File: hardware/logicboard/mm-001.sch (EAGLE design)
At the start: 31 parts, among them IC1 74ALS05N, IC2 LTC485N, IC3 LTC485N, J0 DC5V, J7 DIN5, J8 DIN5, J9 DIN5, X7 NELTRON-7810-XPXC, X9 NELTRON-7810-XPXC

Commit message: Trying to fit in to the new platform.
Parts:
- removed J0: DC5V, con-jack:JACK-PLUG0
- removed J7, J8, J9: DIN5, SparkFun-Connectors:DIN5
- removed LED1: BLUE, led:LED3MM
- removed LED2, LED3: YELLOW, led:LED3MM
- removed R7L2, R8L3: 1k, rcl:R-EU_0204/5
- removed X7, X9: NELTRON-7810-XPXC, con-rj45:NELTRON-7810-XPXC
- added JP1, JP2: (no value), pinhead:PINHD-1X6
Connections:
- removed net MTRTN: J8.5, R5.1
- removed net MTSND: J8.4, R4.1
- removed net N$1: IC1C.O, LED2.C
- removed net N$2: LED3.A, R8L3.1
- removed net N$3: IC1F.O, LED3.C
- removed net N$5: LED2.A, R7L2.1
- net GND: now also JP1.1, JP2.1; no longer J0.1, J0.2, J8.2, J9.2, LED1.C, X7.S1, X7.S2, X9.S1, X9.S2
- net MIRTN: now also JP1.4; no longer J7.5
- net MISND: now also JP1.3; no longer J7.4
- net MORTN: now also JP1.6; no longer J9.5
- net MOSND: now also JP1.5; no longer J9.4
- net N$4: now also JP2.2; no longer LED1.A
- net RX+: now also JP2.5; no longer X7.1
- net RX-: now also JP2.6; no longer X7.2
- net TX+: now also JP2.3; no longer X9.1
- net TX-: now also JP2.4; no longer X9.2
- net VCC: now also JP1.2; no longer J0.3, R7L2.2, R8L3.2
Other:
- moved on the sheet: R6L1

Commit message: First try.
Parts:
- removed R5: 220, rcl:R-EU_0204/5
- R4: value 220 -> 100
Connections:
- removed net MIDITHRU: IC1B.O, R5.2
- removed net NMIDITHRU: IC1A.O, IC1B.I, RN2.3
- net GND: now also IC1A.I, IC1B.I, IC1C.I, IC1F.I
- net RX: no longer IC1F.I
- net TX: no longer IC1A.I, IC1C.I
- net TX+: now also R4.1
- net TX-: now also R4.2
- net VCC: no longer R4.2
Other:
- moved on the sheet: IC1A, IC1B, IC1C, IC1F, R4

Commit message: Artwork.
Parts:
- JP2: device pinhead:PINHD-1X6 -> pinhead:PINHD-1X8
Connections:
- new net V+: JP1.2, JP2.1
- net GND: now also JP2.3; no longer JP2.1
- net N$4: now also JP2.4; no longer JP2.2
- net RX+: now also JP2.7; no longer JP2.5
- net RX-: now also JP2.8; no longer JP2.6
- net TX+: now also JP2.5; no longer JP2.3
- net TX-: now also JP2.6; no longer JP2.4
- net VCC: now also JP2.2; no longer JP1.2
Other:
- moved on the sheet: R6L1
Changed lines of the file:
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@@
 <part name="R3" library="rcl" library_urn="urn:adsk.eagle:library:334" deviceset="R-EU_" device="0204/5" package3d_urn="urn:adsk.eagle:package:23488/1" value="220"/>
 <part name="SUPPLY22" library="supply2" library_urn="urn:adsk.eagle:library:372" deviceset="GND" device=""/>
-<part name="SUPPLY23" library="supply2" library_urn="urn:adsk.eagle:library:372" deviceset="VCC" device=""/>
 <part name="SUPPLY25" library="supply2" library_urn="urn:adsk.eagle:library:372" deviceset="GND" device=""/>
 <part name="JP1" library="pinhead" library_urn="urn:adsk.eagle:library:325" deviceset="PINHD-1X6" device="" package3d_urn="urn:adsk.eagle:package:22472/2"/>
-<part name="JP2" library="pinhead" library_urn="urn:adsk.eagle:library:325" deviceset="PINHD-1X6" device="" package3d_urn="urn:adsk.eagle:package:22472/2"/>
+<part name="JP2" library="pinhead" library_urn="urn:adsk.eagle:library:325" deviceset="PINHD-1X8" device="" package3d_urn="urn:adsk.eagle:package:22409/2"/>
 <part name="SUPPLY1" library="supply2" library_urn="urn:adsk.eagle:library:372" deviceset="GND" device=""/>
 <part name="R4" library="rcl" library_urn="urn:adsk.eagle:library:334" deviceset="R-EU_" device="0204/5" package3d_urn="urn:adsk.eagle:package:23488/1" value="100"/>
@@
 <attribute name="VALUE" x="74.295" y="6.985" size="1.778" layer="96"/>
 </instance>
-<instance part="SUPPLY28" gate="G$1" x="210.82" y="154.94" smashed="yes">
-<attribute name="VALUE" x="208.915" y="158.115" size="1.778" layer="96"/>
+<instance part="SUPPLY28" gate="G$1" x="208.28" y="157.48" smashed="yes">
+<attribute name="VALUE" x="206.375" y="160.655" size="1.778" layer="96"/>
 </instance>
 <instance part="R9" gate="G$1" x="182.88" y="66.04" smashed="yes">
@@
 <attribute name="VALUE" x="179.07" y="62.738" size="1.778" layer="96"/>
 </instance>
-<instance part="R6L1" gate="G$1" x="210.82" y="144.78" smashed="yes" rot="R90">
-<attribute name="NAME" x="209.3214" y="140.97" size="1.778" layer="95" rot="R90"/>
-<attribute name="VALUE" x="214.122" y="140.97" size="1.778" layer="96" rot="R90"/>
+<instance part="R6L1" gate="G$1" x="208.28" y="144.78" smashed="yes" rot="R90">
+<attribute name="NAME" x="206.7814" y="140.97" size="1.778" layer="95" rot="R90"/>
+<attribute name="VALUE" x="211.582" y="140.97" size="1.778" layer="96" rot="R90"/>
 </instance>
 <instance part="R1" gate="G$1" x="76.2" y="127" smashed="yes">
@@
 <attribute name="VALUE" x="15.875" y="78.105" size="1.778" layer="96"/>
 </instance>
-<instance part="SUPPLY23" gate="G$1" x="17.78" y="129.54" smashed="yes">
-<attribute name="VALUE" x="15.875" y="132.715" size="1.778" layer="96"/>
-</instance>
 <instance part="SUPPLY25" gate="GND" x="213.36" y="109.22" smashed="yes">
 <attribute name="VALUE" x="211.455" y="106.045" size="1.778" layer="96"/>
@@
 <attribute name="VALUE" x="13.97" y="109.22" size="1.778" layer="96" rot="R180"/>
 </instance>
-<instance part="JP2" gate="A" x="223.52" y="127" smashed="yes">
-<attribute name="NAME" x="217.17" y="137.795" size="1.778" layer="95"/>
-<attribute name="VALUE" x="217.17" y="116.84" size="1.778" layer="96"/>
+<instance part="JP2" gate="A" x="223.52" y="129.54" smashed="yes">
+<attribute name="NAME" x="217.17" y="140.335" size="1.778" layer="95"/>
+<attribute name="VALUE" x="217.17" y="119.38" size="1.778" layer="96"/>
 </instance>
 <instance part="SUPPLY1" gate="GND" x="218.44" y="45.72" smashed="yes">
@@
 </segment>
 <segment>
-<wire x1="220.98" y1="134.62" x2="213.36" y2="134.62" width="0.1524" layer="91"/>
 <wire x1="213.36" y1="134.62" x2="213.36" y2="111.76" width="0.1524" layer="91"/>
 <pinref part="SUPPLY25" gate="GND" pin="GND"/>
-<pinref part="JP2" gate="A" pin="1"/>
+<pinref part="JP2" gate="A" pin="3"/>
+<wire x1="220.98" y1="134.62" x2="213.36" y2="134.62" width="0.1524" layer="91"/>
 </segment>
 <segment>
@@
 <pinref part="SUPPLY28" gate="G$1" pin="VCC"/>
 <pinref part="R6L1" gate="G$1" pin="2"/>
-<wire x1="210.82" y1="152.4" x2="210.82" y2="149.86" width="0.1524" layer="91"/>
-</segment>
-<segment>
-<wire x1="10.16" y1="93.98" x2="17.78" y2="93.98" width="0.1524" layer="91"/>
-<wire x1="17.78" y1="93.98" x2="17.78" y2="127" width="0.1524" layer="91"/>
-<pinref part="SUPPLY23" gate="G$1" pin="VCC"/>
-<pinref part="JP1" gate="A" pin="2"/>
+<wire x1="208.28" y1="154.94" x2="208.28" y2="152.4" width="0.1524" layer="91"/>
+<wire x1="208.28" y1="152.4" x2="208.28" y2="149.86" width="0.1524" layer="91"/>
+<wire x1="208.28" y1="152.4" x2="210.82" y2="152.4" width="0.1524" layer="91"/>
+<junction x="208.28" y="152.4"/>
+<pinref part="JP2" gate="A" pin="2"/>
+<wire x1="210.82" y1="152.4" x2="210.82" y2="137.16" width="0.1524" layer="91"/>
+<wire x1="210.82" y1="137.16" x2="220.98" y2="137.16" width="0.1524" layer="91"/>
 </segment>
 </net>
@@
 <wire x1="165.1" y1="129.54" x2="172.72" y2="129.54" width="0.1524" layer="91"/>
 <label x="167.64" y="129.54" size="1.778" layer="95"/>
-<pinref part="JP2" gate="A" pin="3"/>
 <pinref part="R4" gate="G$1" pin="1"/>
-<wire x1="172.72" y1="129.54" x2="220.98" y2="129.54" width="0.1524" layer="91"/>
 <wire x1="175.26" y1="134.62" x2="172.72" y2="134.62" width="0.1524" layer="91"/>
 <wire x1="172.72" y1="134.62" x2="172.72" y2="129.54" width="0.1524" layer="91"/>
+<pinref part="JP2" gate="A" pin="5"/>
+<wire x1="220.98" y1="129.54" x2="172.72" y2="129.54" width="0.1524" layer="91"/>
 <junction x="172.72" y="129.54"/>
 </segment>
@@
 <wire x1="175.26" y1="66.04" x2="175.26" y2="60.96" width="0.1524" layer="91"/>
 <junction x="175.26" y="60.96"/>
+<wire x1="203.2" y1="124.46" x2="203.2" y2="60.96" width="0.1524" layer="91"/>
+<pinref part="JP2" gate="A" pin="7"/>
 <wire x1="220.98" y1="124.46" x2="203.2" y2="124.46" width="0.1524" layer="91"/>
-<wire x1="203.2" y1="124.46" x2="203.2" y2="60.96" width="0.1524" layer="91"/>
-<pinref part="JP2" gate="A" pin="5"/>
 </segment>
 </net>
@@
 <wire x1="165.1" y1="127" x2="187.96" y2="127" width="0.1524" layer="91"/>
 <label x="167.64" y="127" size="1.778" layer="95"/>
-<pinref part="JP2" gate="A" pin="4"/>
 <pinref part="R4" gate="G$1" pin="2"/>
-<wire x1="187.96" y1="127" x2="220.98" y2="127" width="0.1524" layer="91"/>
 <wire x1="185.42" y1="134.62" x2="187.96" y2="134.62" width="0.1524" layer="91"/>
 <wire x1="187.96" y1="134.62" x2="187.96" y2="127" width="0.1524" layer="91"/>
+<pinref part="JP2" gate="A" pin="6"/>
+<wire x1="220.98" y1="127" x2="187.96" y2="127" width="0.1524" layer="91"/>
 <junction x="187.96" y="127"/>
 </segment>
@@
 <wire x1="190.5" y1="66.04" x2="190.5" y2="58.42" width="0.1524" layer="91"/>
 <junction x="190.5" y="58.42"/>
-<wire x1="220.98" y1="121.92" x2="205.74" y2="121.92" width="0.1524" layer="91"/>
 <wire x1="205.74" y1="121.92" x2="205.74" y2="58.42" width="0.1524" layer="91"/>
 <wire x1="205.74" y1="58.42" x2="190.5" y2="58.42" width="0.1524" layer="91"/>
-<pinref part="JP2" gate="A" pin="6"/>
+<pinref part="JP2" gate="A" pin="8"/>
+<wire x1="220.98" y1="121.92" x2="205.74" y2="121.92" width="0.1524" layer="91"/>
 </segment>
 </net>
@@
 <segment>
 <pinref part="R6L1" gate="G$1" pin="1"/>
-<wire x1="210.82" y1="139.7" x2="210.82" y2="132.08" width="0.1524" layer="91"/>
-<wire x1="220.98" y1="132.08" x2="210.82" y2="132.08" width="0.1524" layer="91"/>
-<pinref part="JP2" gate="A" pin="2"/>
-</segment>
-</net>
+<wire x1="208.28" y1="139.7" x2="208.28" y2="132.08" width="0.1524" layer="91"/>
+<pinref part="JP2" gate="A" pin="4"/>
+<wire x1="208.28" y1="132.08" x2="220.98" y2="132.08" width="0.1524" layer="91"/>
+</segment>
+</net>
+<net name="V+" class="2">
+<segment>
+<pinref part="JP2" gate="A" pin="1"/>
+<wire x1="220.98" y1="139.7" x2="213.36" y2="139.7" width="0.1524" layer="91"/>
+<wire x1="213.36" y1="139.7" x2="213.36" y2="154.94" width="0.1524" layer="91"/>
+<label x="213.36" y="154.94" size="0.8128" layer="95" rot="R90" xref="yes"/>
+</segment>
+<segment>
+<wire x1="10.16" y1="93.98" x2="17.78" y2="93.98" width="0.1524" layer="91"/>
+<wire x1="17.78" y1="93.98" x2="17.78" y2="129.54" width="0.1524" layer="91"/>
+<pinref part="JP1" gate="A" pin="2"/>
+<label x="17.78" y="129.54" size="0.8128" layer="95" rot="R90" xref="yes"/>
+</segment>
+</net>

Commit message: Mostly done.
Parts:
- removed R6L1: 1k, rcl:R-EU_0204/5
- added R6: 100, rcl:R-EU_0204/5
- C1: value 100n -> 10n
- C3: value 10n -> 100n
- JP1: value (none) -> Backside
- JP2: value (none) -> Frontside
- R4: value 100 -> 1k
- renumbered R9 to R5, RN2 to RN1
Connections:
- removed net N$4: JP2.4, R6L1.1
- new net LED: JP2.4, R4.1
- net GND: now also JP2.1; no longer JP2.3
- net TX+: now also R6.1; no longer R4.1
- net TX-: now also R6.2; no longer R4.2
- net V+: now also JP2.2; no longer JP2.1
- net VCC: now also JP2.3, R4.2; no longer JP2.2, R6L1.2
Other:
- note removed: "MIDI IN"
- note removed: "MIDI OUT"
- note removed: "MIDI THRU"
- moved on the sheet: C1, C2, C3, C4, R4

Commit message: Rebuild.
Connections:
- net RX+: now also JP2.5; no longer JP2.7
- net RX-: now also JP2.6; no longer JP2.8
- net TX+: now also JP2.7; no longer JP2.5
- net TX-: now also JP2.8; no longer JP2.6
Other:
- moved on the sheet: JP2
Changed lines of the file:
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@@
 <attribute name="VALUE" x="13.97" y="109.22" size="1.778" layer="96" rot="R180"/>
 </instance>
-<instance part="JP2" gate="A" x="223.52" y="129.54" smashed="yes">
-<attribute name="NAME" x="217.17" y="140.335" size="1.778" layer="95"/>
-<attribute name="VALUE" x="217.17" y="119.38" size="1.778" layer="96"/>
+<instance part="JP2" gate="A" x="226.06" y="134.62" smashed="yes">
+<attribute name="NAME" x="219.71" y="145.415" size="1.778" layer="95"/>
+<attribute name="VALUE" x="219.71" y="124.46" size="1.778" layer="96"/>
 </instance>
 <instance part="SUPPLY1" gate="GND" x="218.44" y="45.72" smashed="yes">
@@
 </segment>
 <segment>
-<wire x1="215.9" y1="139.7" x2="215.9" y2="111.76" width="0.1524" layer="91"/>
+<wire x1="215.9" y1="144.78" x2="215.9" y2="111.76" width="0.1524" layer="91"/>
 <pinref part="SUPPLY25" gate="GND" pin="GND"/>
 <pinref part="JP2" gate="A" pin="1"/>
-<wire x1="220.98" y1="139.7" x2="215.9" y2="139.7" width="0.1524" layer="91"/>
+<wire x1="223.52" y1="144.78" x2="215.9" y2="144.78" width="0.1524" layer="91"/>
 </segment>
 <segment>
@@
 <wire x1="208.28" y1="152.4" x2="210.82" y2="152.4" width="0.1524" layer="91"/>
 <junction x="208.28" y="152.4"/>
-<wire x1="210.82" y1="152.4" x2="210.82" y2="134.62" width="0.1524" layer="91"/>
+<wire x1="210.82" y1="152.4" x2="210.82" y2="139.7" width="0.1524" layer="91"/>
 <pinref part="JP2" gate="A" pin="3"/>
-<wire x1="220.98" y1="134.62" x2="210.82" y2="134.62" width="0.1524" layer="91"/>
+<wire x1="223.52" y1="139.7" x2="210.82" y2="139.7" width="0.1524" layer="91"/>
 </segment>
 </net>
@@
 <wire x1="175.26" y1="134.62" x2="172.72" y2="134.62" width="0.1524" layer="91"/>
 <wire x1="172.72" y1="134.62" x2="172.72" y2="129.54" width="0.1524" layer="91"/>
-<pinref part="JP2" gate="A" pin="5"/>
-<wire x1="220.98" y1="129.54" x2="172.72" y2="129.54" width="0.1524" layer="91"/>
+<pinref part="JP2" gate="A" pin="7"/>
+<wire x1="223.52" y1="129.54" x2="172.72" y2="129.54" width="0.1524" layer="91"/>
 <junction x="172.72" y="129.54"/>
 </segment>
@@
 <wire x1="175.26" y1="66.04" x2="175.26" y2="60.96" width="0.1524" layer="91"/>
 <junction x="175.26" y="60.96"/>
-<wire x1="203.2" y1="124.46" x2="203.2" y2="60.96" width="0.1524" layer="91"/>
-<pinref part="JP2" gate="A" pin="7"/>
-<wire x1="220.98" y1="124.46" x2="203.2" y2="124.46" width="0.1524" layer="91"/>
+<wire x1="203.2" y1="134.62" x2="203.2" y2="60.96" width="0.1524" layer="91"/>
+<pinref part="JP2" gate="A" pin="5"/>
+<wire x1="223.52" y1="134.62" x2="203.2" y2="134.62" width="0.1524" layer="91"/>
 </segment>
 </net>
@@
 <wire x1="185.42" y1="134.62" x2="187.96" y2="134.62" width="0.1524" layer="91"/>
 <wire x1="187.96" y1="134.62" x2="187.96" y2="127" width="0.1524" layer="91"/>
-<pinref part="JP2" gate="A" pin="6"/>
-<wire x1="220.98" y1="127" x2="187.96" y2="127" width="0.1524" layer="91"/>
+<pinref part="JP2" gate="A" pin="8"/>
+<wire x1="223.52" y1="127" x2="187.96" y2="127" width="0.1524" layer="91"/>
 <junction x="187.96" y="127"/>
 </segment>
@@
 <wire x1="190.5" y1="66.04" x2="190.5" y2="58.42" width="0.1524" layer="91"/>
 <junction x="190.5" y="58.42"/>
-<wire x1="205.74" y1="121.92" x2="205.74" y2="58.42" width="0.1524" layer="91"/>
+<wire x1="205.74" y1="132.08" x2="205.74" y2="58.42" width="0.1524" layer="91"/>
 <wire x1="205.74" y1="58.42" x2="190.5" y2="58.42" width="0.1524" layer="91"/>
-<pinref part="JP2" gate="A" pin="8"/>
-<wire x1="220.98" y1="121.92" x2="205.74" y2="121.92" width="0.1524" layer="91"/>
+<pinref part="JP2" gate="A" pin="6"/>
+<wire x1="223.52" y1="132.08" x2="205.74" y2="132.08" width="0.1524" layer="91"/>
 </segment>
 </net>
@@
 <segment>
 <pinref part="R4" gate="G$1" pin="1"/>
-<wire x1="208.28" y1="139.7" x2="208.28" y2="132.08" width="0.1524" layer="91"/>
+<wire x1="208.28" y1="139.7" x2="208.28" y2="137.16" width="0.1524" layer="91"/>
 <pinref part="JP2" gate="A" pin="4"/>
-<wire x1="220.98" y1="132.08" x2="208.28" y2="132.08" width="0.1524" layer="91"/>
+<wire x1="223.52" y1="137.16" x2="208.28" y2="137.16" width="0.1524" layer="91"/>
 </segment>
 </net>
 <net name="V+" class="2">
 <segment>
-<wire x1="213.36" y1="137.16" x2="213.36" y2="154.94" width="0.1524" layer="91"/>
+<wire x1="213.36" y1="142.24" x2="213.36" y2="154.94" width="0.1524" layer="91"/>
 <label x="213.36" y="154.94" size="0.8128" layer="95" rot="R90" xref="yes"/>
 <pinref part="JP2" gate="A" pin="2"/>
-<wire x1="220.98" y1="137.16" x2="213.36" y2="137.16" width="0.1524" layer="91"/>
-</segment>
-<segment>
+<wire x1="223.52" y1="142.24" x2="213.36" y2="142.24" width="0.1524" layer="91"/>
+</segment>
+<segment>

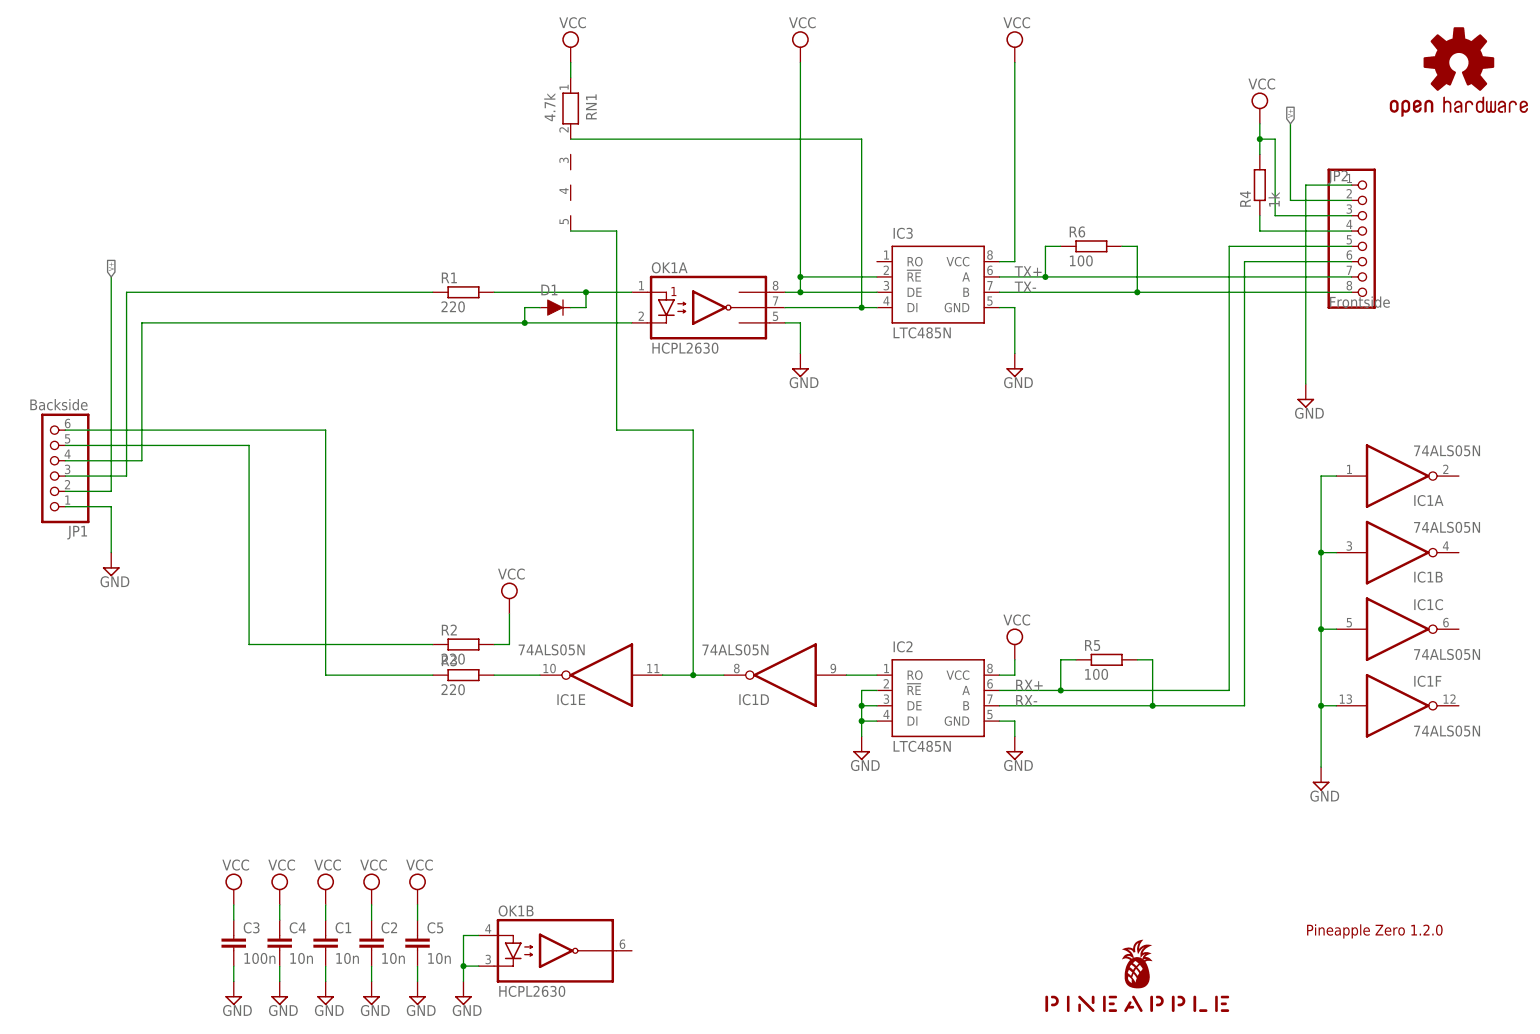
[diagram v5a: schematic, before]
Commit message: Added test leds.
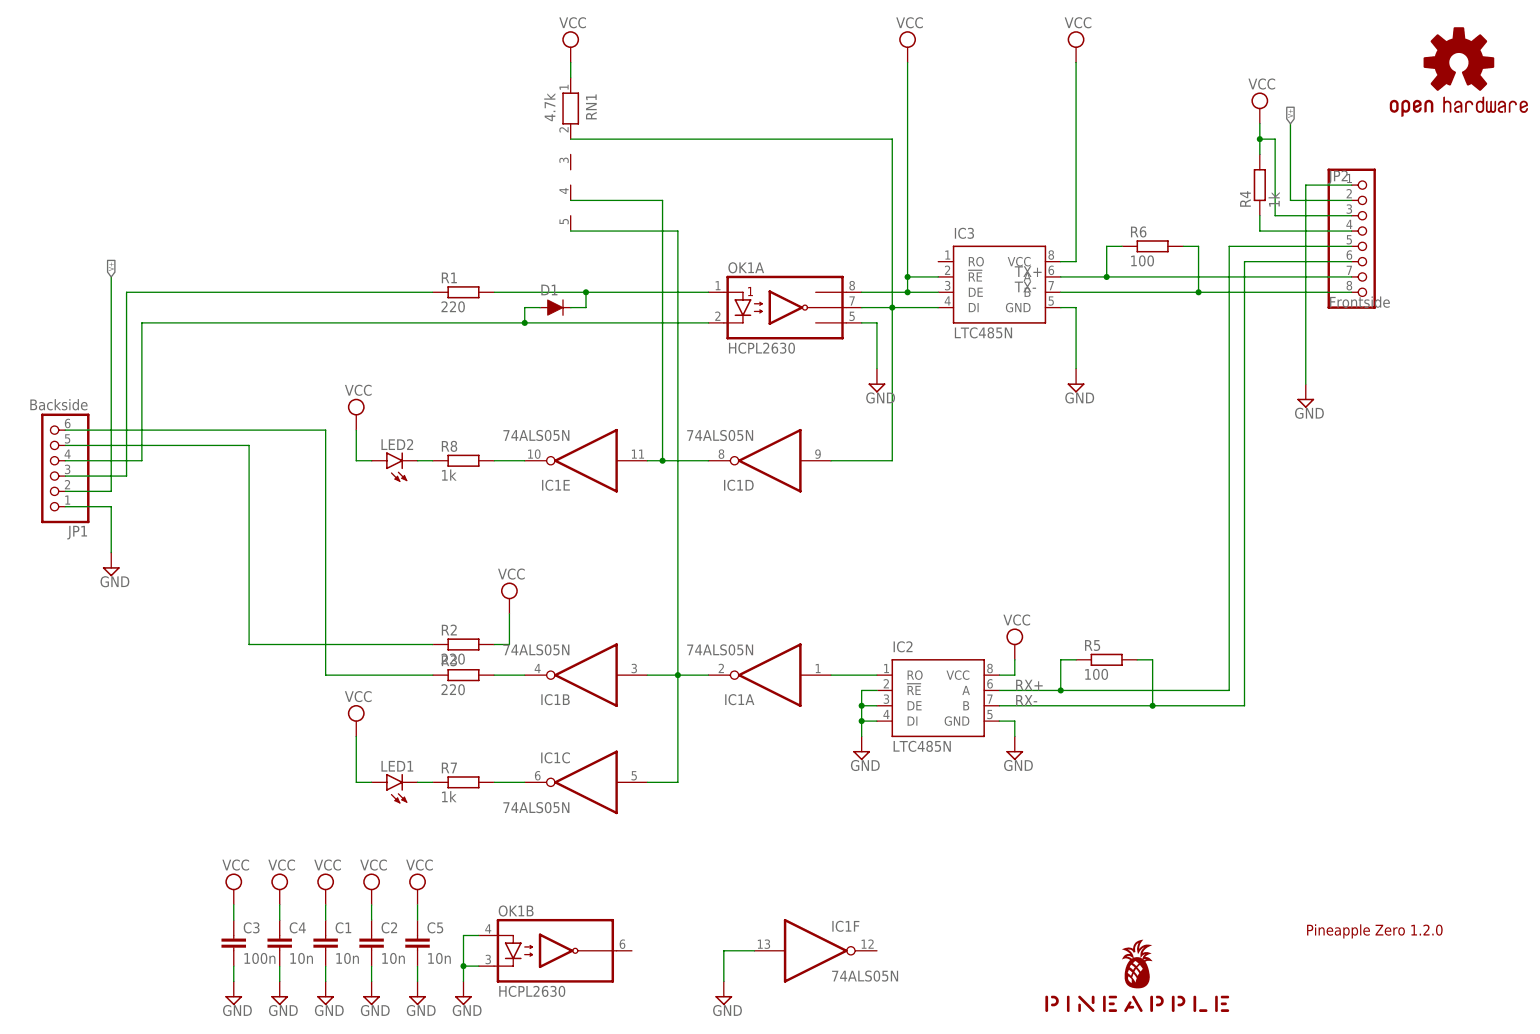
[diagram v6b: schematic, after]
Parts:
- added LED1, LED2: (no value), led:LED3MM
- added R7, R8: 1k, rcl:R-EU_0204/5
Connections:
- removed net MIDIOUT: IC1E.O, R3.2
- removed net RX: IC1D.I, IC2.RO
- new net LED1: IC1C.O, R7.2
- new net LED1K: LED1.C, R7.1
- new net LED2: IC1E.O, R8.2
- new net LED2K: LED2.C, R8.1
- new net N$1: IC1A.I, IC2.RO
- new net N$2: IC1B.O, R3.2
- new net N$5: IC1D.O, IC1E.I, RN1.4
- net GND: no longer IC1A.I, IC1B.I, IC1C.I
- net NMIDIOUT: now also IC1A.O, IC1B.I, IC1C.I; no longer IC1D.O, IC1E.I
- net TX: now also IC1D.I
- net VCC: now also LED1.A, LED2.A
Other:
- moved on the sheet: IC1A, IC1B, IC1C, IC1D, IC1E, IC1F, IC3, OK1A, R6
